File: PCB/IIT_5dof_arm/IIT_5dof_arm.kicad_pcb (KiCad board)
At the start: 2 copper layers, 100 x 100 mm, 45 parts, among them J1 Screw_Terminal_01x02, J2 Conn_01x06, J3 Conn_01x06, J4 Conn_01x06, J5 Conn_01x06, J6 Conn_01x06, J7 Conn_01x06, J9 DE9_Receptacle_MountingHoles, SW1 SW_MAIN, SW15 SW_MOT, U5 XL8574T, U6 MAX3232, U9 4504

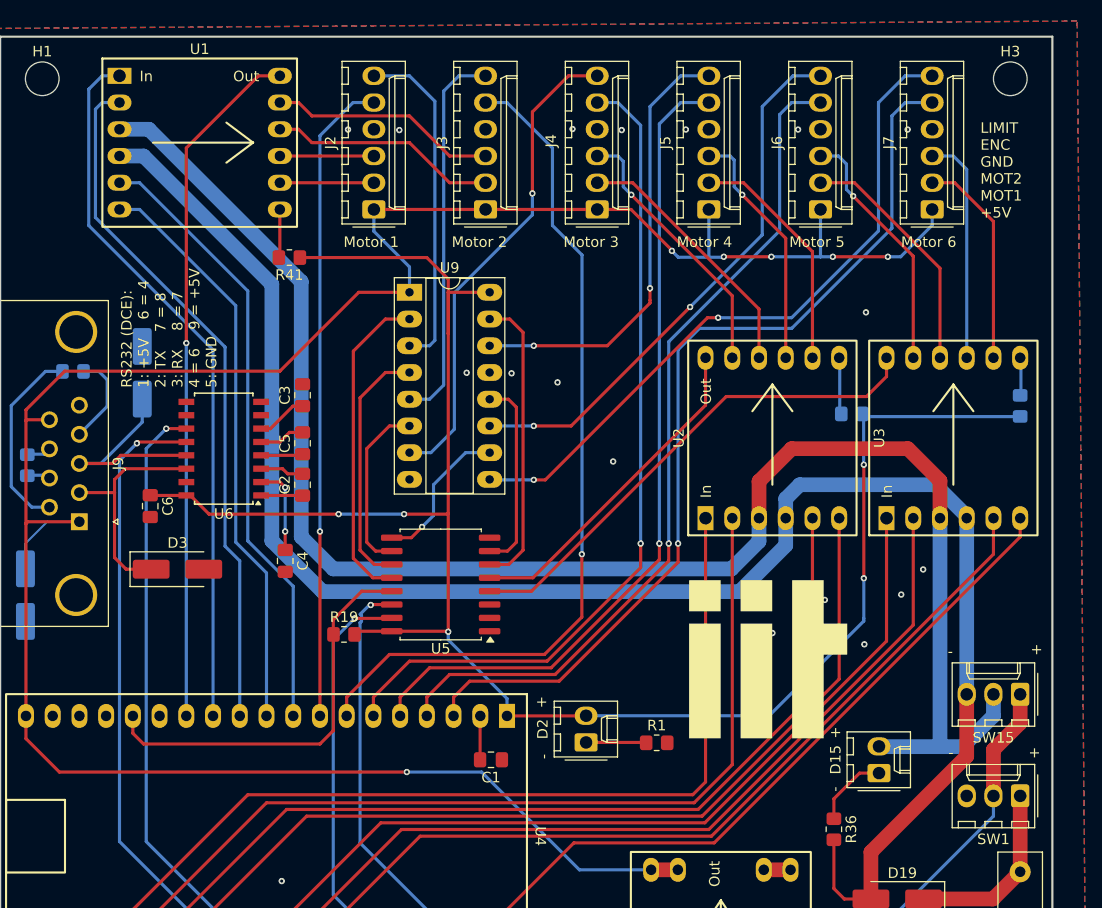
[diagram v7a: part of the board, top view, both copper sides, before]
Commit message: Decoupling capacitors layout
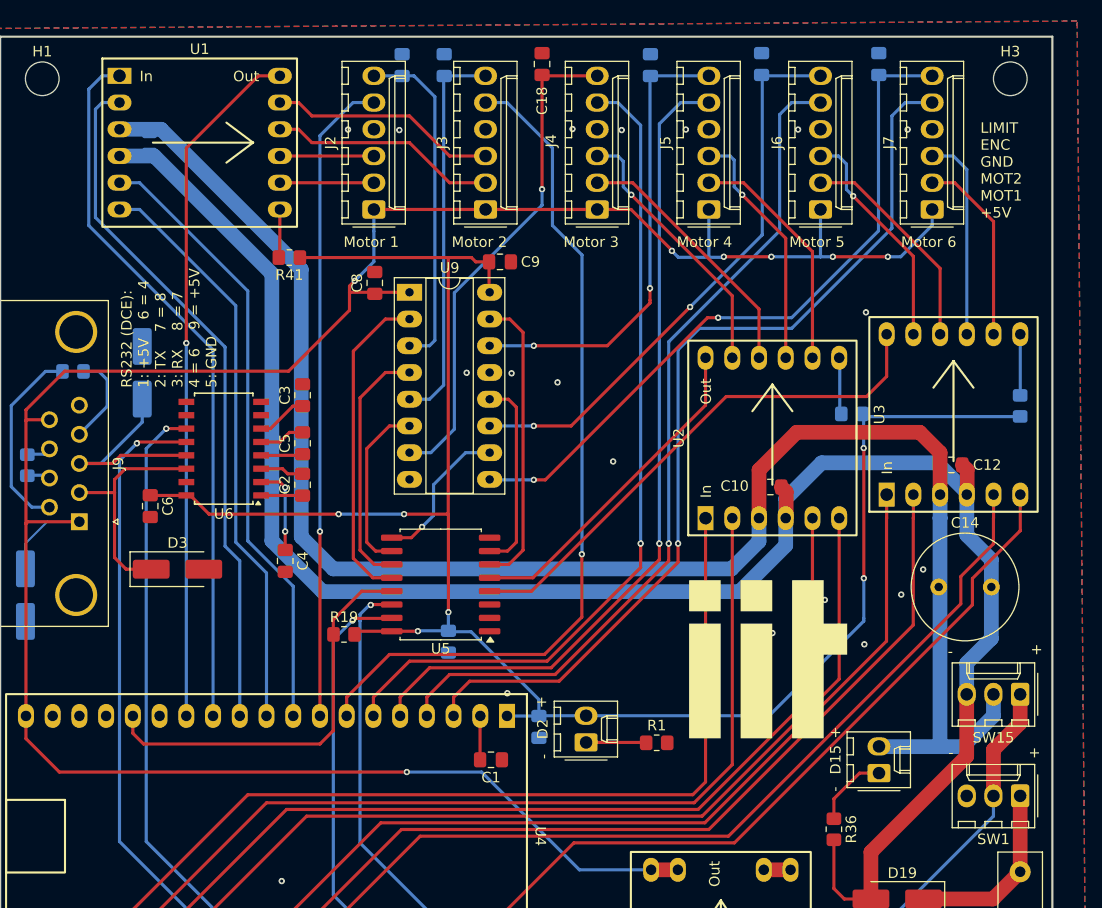
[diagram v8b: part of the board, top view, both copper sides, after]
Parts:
- added C10: 0.1uF, Capacitor_SMD:C_0805_2012Metric_Pad1.18x1.45mm_HandSolder, F.Cu at (123.2, 92.8)
- added C11: 0.1uF, Capacitor_SMD:C_0805_2012Metric_Pad1.18x1.45mm_HandSolder, B.Cu at (64.2, 60.1)
- added C12: 0.1uF, Capacitor_SMD:C_0805_2012Metric_Pad1.18x1.45mm_HandSolder, F.Cu at (140.4, 90.7)
- added C13: 0.1uF, Capacitor_SMD:C_0805_2012Metric_Pad1.18x1.45mm_HandSolder, B.Cu at (101.2, 115.6)
- added C14: 1000uF, Capacitor_THT:C_Radial_D10.0mm_H16.0mm_P5.00mm, F.Cu at (139.2, 102.3)
- added C15: 10nF, Capacitor_SMD:C_0805_2012Metric_Pad1.18x1.45mm_HandSolder, B.Cu at (111.8, 52.7)
- added C16: 10nF, Capacitor_SMD:C_0805_2012Metric_Pad1.18x1.45mm_HandSolder, B.Cu at (122.4, 52.6)
- added C17: 10nF, Capacitor_SMD:C_0805_2012Metric_Pad1.18x1.45mm_HandSolder, B.Cu at (92.2, 52.7)
- added C18: 10nF, Capacitor_SMD:C_0805_2012Metric_Pad1.18x1.45mm_HandSolder, F.Cu at (101.5, 52.6)
- added C19: 10nF, Capacitor_SMD:C_0805_2012Metric_Pad1.18x1.45mm_HandSolder, B.Cu at (133.5, 52.6)
- added C20: 10nF, Capacitor_SMD:C_0805_2012Metric_Pad1.18x1.45mm_HandSolder, B.Cu at (88.2, 52.7)
- added C7: 0.1uF, Capacitor_SMD:C_0805_2012Metric_Pad1.18x1.45mm_HandSolder, B.Cu at (92.6, 107.5)
- added C8: 0.1uF, Capacitor_SMD:C_0805_2012Metric_Pad1.18x1.45mm_HandSolder, F.Cu at (85.6, 73.4)
- added C9: 0.1uF, Capacitor_SMD:C_0805_2012Metric_Pad1.18x1.45mm_HandSolder, F.Cu at (97.5, 71.4)
- moved U3 2.24 mm to (140.6, 85.9)
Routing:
- net GNDPWR: track 193.1 -> 204.8 mm
- net VCC: track 158.3 -> 162.5 mm
- net /mot6_B: track 70.7 -> 74.1 mm
- net +3V3: track 177.0 -> 180.3 mm, vias 5 -> 6
- net /mot6_A: track 84.4 -> 87.6 mm
- net /mot5_B: track 83.2 -> 85.4 mm
- net /mot5_A: track 84.1 -> 86.3 mm
- net /~{Fault}_56: track 48.0 -> 50.2 mm
- net /Mot6_OUT1: track 20.3 -> 18.1 mm
- net /Mot6_OUT2: track 21.7 -> 19.5 mm
- net /Mot5_OUT2: track 23.8 -> 21.6 mm
- net /Mot5_OUT1: track 23.2 -> 21.0 mm
- net /~{Sleep}_56: track 3.60 -> 5.81 mm
- net /Mot5_LIMIT_IN: track 52.4 -> 54.3 mm
- net /Mot4_LIMIT_IN: track 42.4 -> 44.1 mm
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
